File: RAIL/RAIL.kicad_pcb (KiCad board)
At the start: 4 copper layers, 93 x 93 mm, 1 part

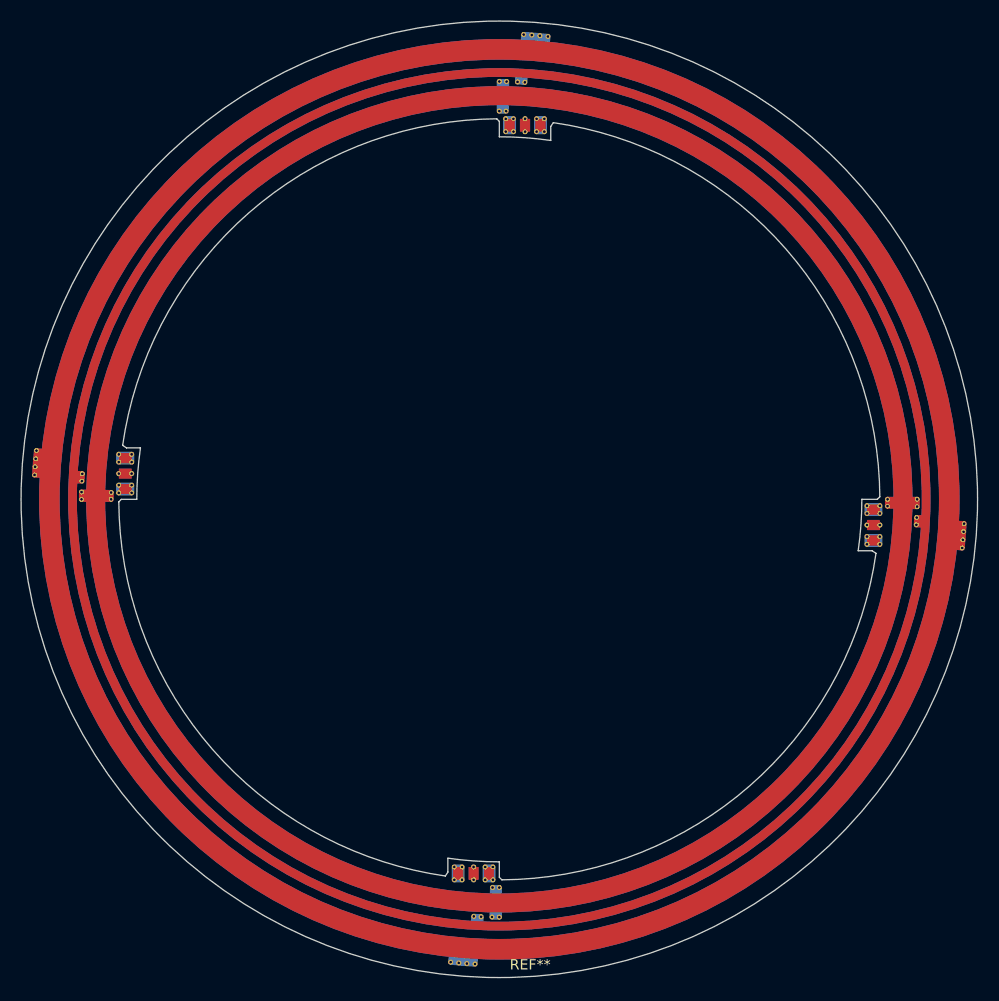
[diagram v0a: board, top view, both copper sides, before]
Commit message: Update designation.
Update CONTACTOR and RAIL.
Add INNER_HOLDER.
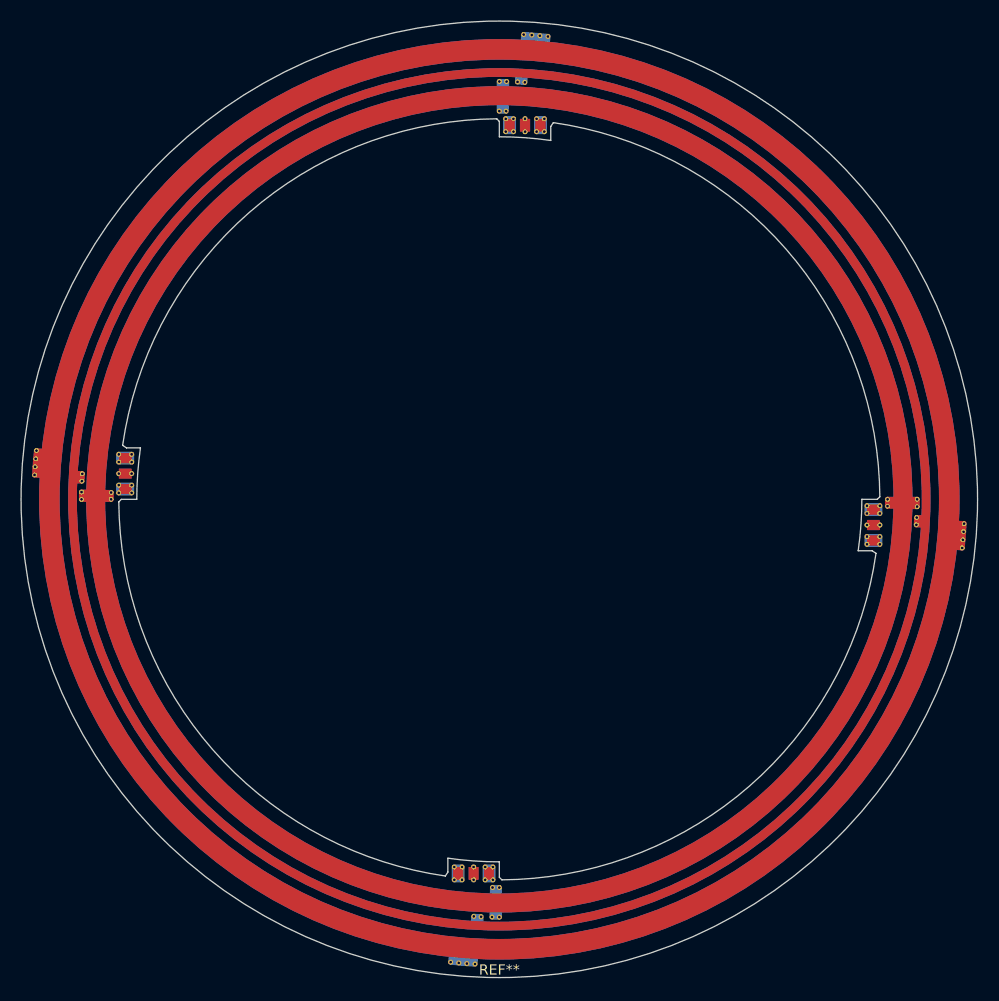
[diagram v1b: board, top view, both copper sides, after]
